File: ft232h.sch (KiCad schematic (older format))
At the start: 0 parts

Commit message: Add schematic of FT232H. Not placed yet.
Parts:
- added C101, C107, C109: 4.7u, Capacitors_SMD:C_0603, symbol C
- added C102, C103, C104, C106, C108, C36, C38, C53, C84: 100n, Capacitors_SMD:C_0603, symbol C
- added C105: 10n, Capacitors_SMD:C_0603, symbol C
- added C110, C111: 20p, Capacitors_SMD:C_0603, symbol C
- added J3: USB_OTG, Connectors:USB_Mini-B, symbol USB_OTG
- added L13, L14: BLM18KG601SN1D, Inductors_SMD:L_0805, symbol Ferrite_Bead
- added R30, R31, R32, R37: 10k, Resistors_SMD:R_0603, symbol R
- added R35: 2k, Resistors_SMD:R_0603, symbol R
- added R36: 12k 1%, Resistors_SMD:R_0603, symbol R
- added U14: FT232HL, Housings_QFP:LQFP-48_7x7mm_Pitch0.5mm, symbol FT232H
- added U15: 93LCxxBT-I/OT, TO_SOT_Packages_SMD:SOT-23-6, symbol 93LCxxBT-I/OT
- added Y3: ABLS2-12.000MHZ-D4Y-T, Crystals:Crystal_HC49-SD_SMD, symbol Crystal
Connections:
- new net: C110.1, U14.1 (XCSI), Y3.1
- new net: C111.1, U14.2 (XCSO), Y3.2
- new net: C53.1, U14.37 (VCCA)
- new net: C38.1, U14.38 (VCCCORE)
- new net: C106.1, C107.1, L13.1, U14.40 (VREGIN)
- new net: R35.1, U14.43 (EEDATA), U15.3 (DI)
- new net: R36.2, U14.5 (REF)
- new net: R32.2, R35.2, U15.1 (DO)
- new net: J3.1 (VBUS), L13.2
- new net 3V3_PLL: C108.1, C109.1, L14.1, U14.3 (VPHY), U14.8 (VPLL)
- new net CS: R31.2, U14.45 (EECS), U15.5 (CS)
- new net DM: J3.2 (D-), U14.6 (DM)
- new net DP: J3.3 (D+), U14.7 (DP)
- new net FT232_3V3: C101.1, C102.1, C103.1, C104.1, C36.1, C84.1, L14.2, R30.1, R31.1, R32.1, R37.1, U14.12 (VCCIO), U14.24 (VCCIO), U14.39 (VCCD), U14.46 (VCCIO), U15.6 (VCC)
- new net GNDD: C101.2, C102.2, C103.2, C104.2, C105.2, C106.2, C107.2, C108.2, C109.2, C110.2, C111.2, C36.2, C38.2, C53.2, C84.2, J3.5 (GND), J3.6 (Shield), R36.1, U14.10 (DGND), U14.11 (DGND), U14.22 (DGND), U14.23 (DGND), U14.35 (DGND), U14.36 (DGND), U14.4 (DGND), U14.41 (DGND), U14.42 (TEST), U14.47 (DGND), U14.48 (DGND), U14.9 (DGND), U15.2 (GND)
- new net SCLK: R30.2, U14.44 (EECLK), U15.4 (SCLK)
- new net ~RST: C105.1, R37.2, U14.34 (~RESET)

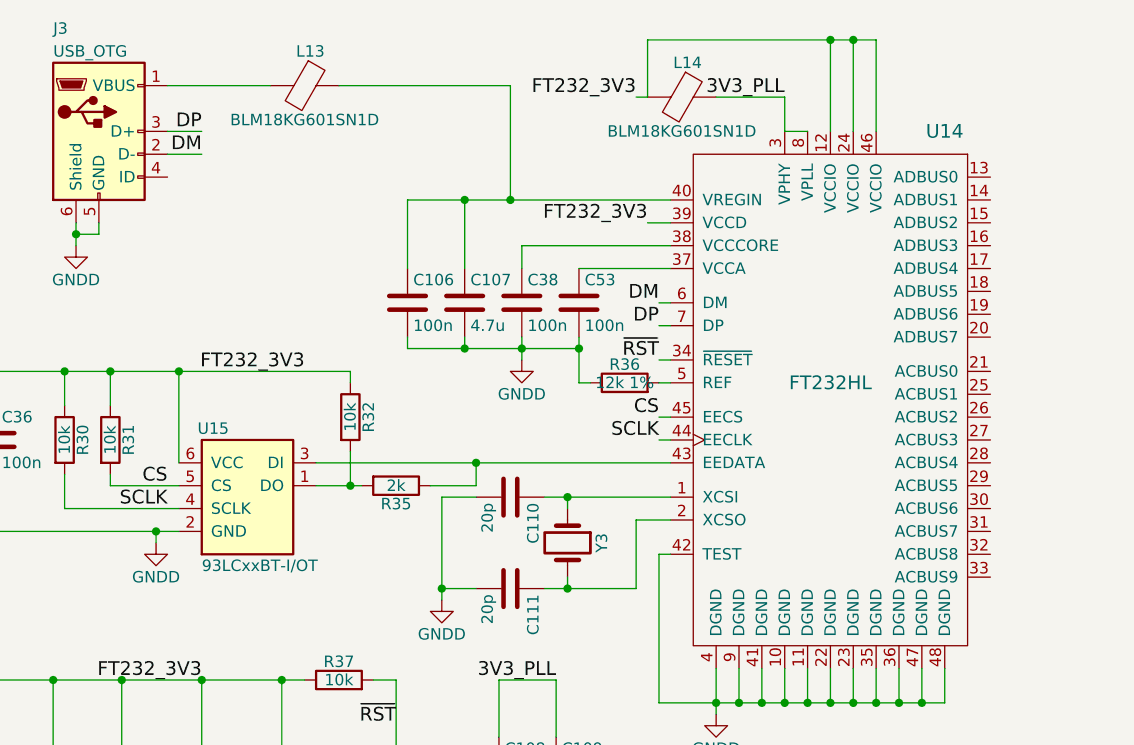
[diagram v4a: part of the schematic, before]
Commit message: FT232H has been finished Not finished: - PROGRAMN button - silkscreen preparation - RF
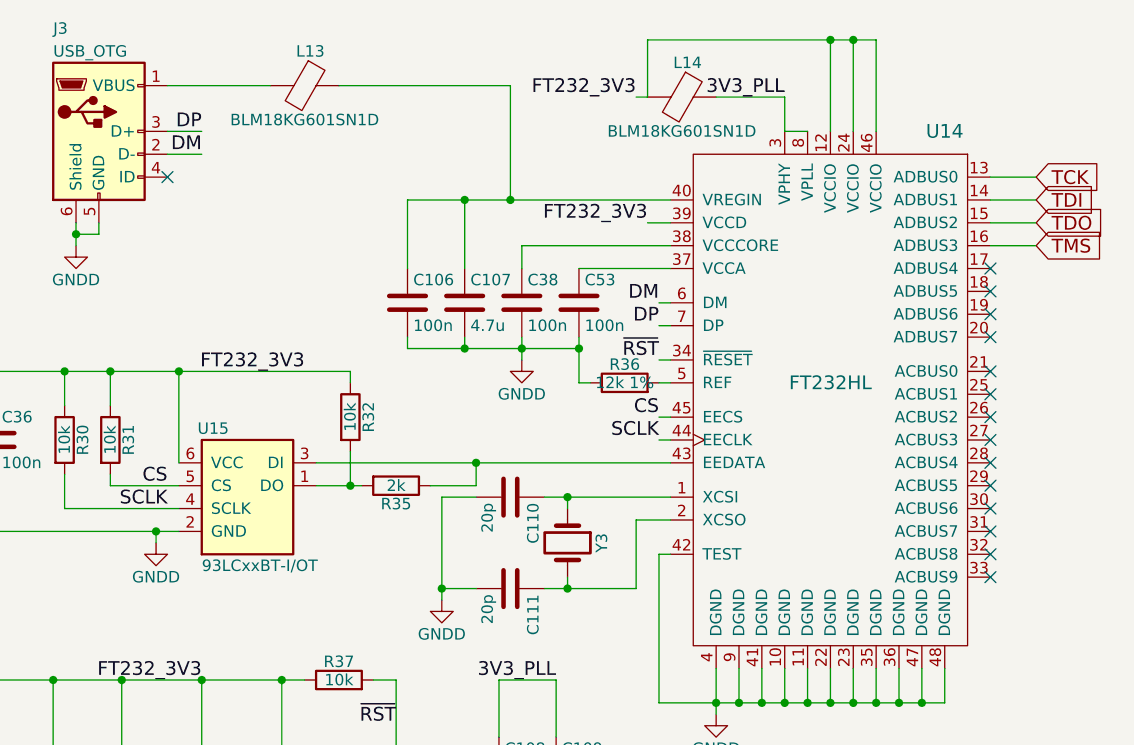
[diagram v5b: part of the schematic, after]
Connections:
- net TCK: now reaches U14.13 (ADBUS0)
- net TDI: now reaches U14.14 (ADBUS1)
- net TDO: now reaches U14.15 (ADBUS2)
- net TMS: now reaches U14.16 (ADBUS3)
- no-connect marks 0 -> 15
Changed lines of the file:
@@
 	3550 3850 3700 3850
 Connection ~ 3250 4150
+Text GLabel 5300 2650 2    60   Input ~ 0
+TMS
+Text GLabel 5300 2450 2    60   Input ~ 0
+TDI
+Text GLabel 5300 2350 2    60   Input ~ 0
+TCK
+Text GLabel 5300 2550 2    60   Input ~ 0
+TDO
+Wire Wire Line
+	5300 2350 5100 2350
+Wire Wire Line
+	5300 2450 5100 2450
+Wire Wire Line
+	5300 2550 5100 2550
+Wire Wire Line
+	5300 2650 5100 2650
+NoConn ~ 5100 2750
+NoConn ~ 5100 2850
+NoConn ~ 5100 2950
+NoConn ~ 5100 3050
+NoConn ~ 5100 3200
+NoConn ~ 5100 3300
+NoConn ~ 5100 3400
+NoConn ~ 5100 3500
+NoConn ~ 5100 3600
+NoConn ~ 5100 3700
+NoConn ~ 5100 3800
+NoConn ~ 5100 3900
+NoConn ~ 5100 4000
+NoConn ~ 5100 4100
+NoConn ~ 1500 2350
 $EndSCHEMATC

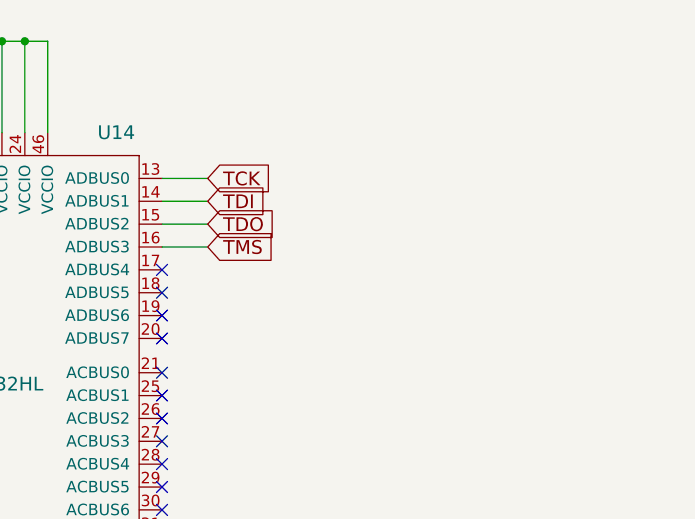
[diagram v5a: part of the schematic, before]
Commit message: Changed JTAG, added 0 Ohm resistors
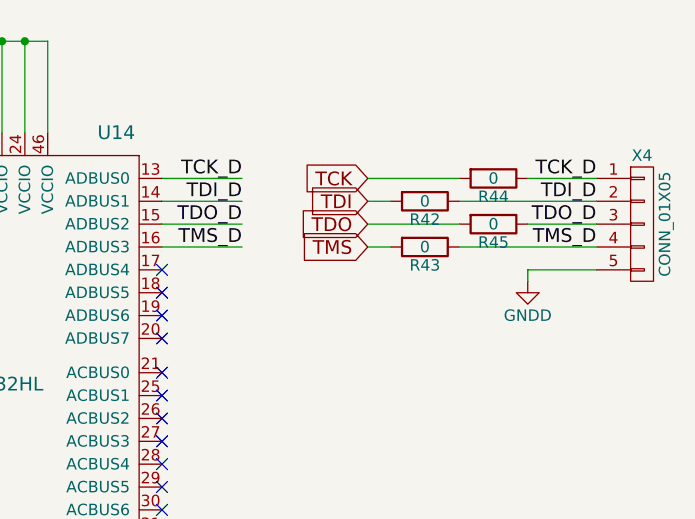
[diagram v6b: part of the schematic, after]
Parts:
- added R42, R43, R44, R45: 0, Resistors_SMD:R_0603, symbol R
- added X4: CONN_01X05, Pin_Headers:Pin_Header_Straight_1x05_Pitch2.00mm, symbol CONN_01X05
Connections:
- net GNDD: now also X4.5 (P5)
- net TCK: now also R44.2; no longer U14.13 (ADBUS0)
- net TDI: now also R42.2; no longer U14.14 (ADBUS1)
- net TDO: now also R45.2; no longer U14.15 (ADBUS2)
- net TMS: now also R43.2; no longer U14.16 (ADBUS3)
- new net TCK_D: R44.1, U14.13 (ADBUS0), X4.1 (P1)
- new net TDI_D: R42.1, U14.14 (ADBUS1), X4.2 (P2)
- new net TDO_D: R45.1, U14.15 (ADBUS2), X4.3 (P3)
- new net TMS_D: R43.1, U14.16 (ADBUS3), X4.4 (P4)
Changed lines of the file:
@@
 	3550 3850 3700 3850
 Connection ~ 3250 4150
-Text GLabel 5300 2650 2    60   Input ~ 0
-TMS
-Text GLabel 5300 2450 2    60   Input ~ 0
-TDI
-Text GLabel 5300 2350 2    60   Input ~ 0
-TCK
-Text GLabel 5300 2550 2    60   Input ~ 0
-TDO
 Wire Wire Line
-	5300 2350 5100 2350
+	5450 2350 5100 2350
 Wire Wire Line
-	5300 2450 5100 2450
+	5450 2450 5100 2450
 Wire Wire Line
-	5300 2550 5100 2550
+	5450 2550 5100 2550
 Wire Wire Line
-	5300 2650 5100 2650
+	5450 2650 5100 2650
 NoConn ~ 5100 2750
 NoConn ~ 5100 2850
@@
 NoConn ~ 5100 4100
 NoConn ~ 1500 2350
+$Comp
+L CONN_01X05 X4
+U 1 1 593E4F67
+P 7200 2550
+F 0 "X4" H 7200 2850 50  0000 C CNN
+F 1 "CONN_01X05" V 7300 2550 50  0000 C CNN
+F 2 "Pin_Headers:Pin_Header_Straight_1x05_Pitch2.00mm" H 7200 2550 50  0001 C CNN
+F 3 "" H 7200 2550 50  0001 C CNN
+	1    7200 2550
+	1    0    0    -1
+$EndComp
+Text GLabel 6000 2650 0    60   Input ~ 0
+TMS
+Text GLabel 6000 2450 0    60   Input ~ 0
+TDI
+Text GLabel 6000 2350 0    60   Input ~ 0
+TCK
+Text GLabel 6000 2550 0    60   Input ~ 0
+TDO
+Wire Wire Line
+	6700 2350 7000 2350
+Wire Wire Line
+	6400 2450 7000 2450
+Wire Wire Line
+	6700 2550 7000 2550
+Wire Wire Line
+	6400 2650 7000 2650
+$Comp
+L GNDD #PWR0104
+U 1 1 593E55E3
+P 6700 2800
+F 0 "#PWR0104" H 6700 2550 50  0001 C CNN
+F 1 "GNDD" H 6700 2650 50  0000 C CNN
+F 2 "" H 6700 2800 50  0001 C CNN
+F 3 "" H 6700 2800 50  0001 C CNN
+	1    6700 2800
+	1    0    0    -1
+$EndComp
+Wire Wire Line
+	6700 2800 6700 2750
+Wire Wire Line
+	6700 2750 7000 2750
+$Comp
+L R R44
+U 1 1 593EA9DA
+P 6550 2350
+F 0 "R44" V 6630 2350 50  0000 C CNN
+F 1 "0" V 6550 2350 50  0000 C CNN
+F 2 "Resistors_SMD:R_0603" V 6480 2350 50  0001 C CNN
+F 3 "" H 6550 2350 50  0001 C CNN
+	1    6550 2350
+	0    1    1    0
+$EndComp
+$Comp
+L R R43
+U 1 1 593EAB87
+P 6250 2650
+F 0 "R43" V 6330 2650 50  0000 C CNN
+F 1 "0" V 6250 2650 50  0000 C CNN
+F 2 "Resistors_SMD:R_0603" V 6180 2650 50  0001 C CNN
+F 3 "" H 6250 2650 50  0001 C CNN
+	1    6250 2650
+	0    1    1    0
+$EndComp
+$Comp
+L R R42
+U 1 1 593EAC51
+P 6250 2450
+F 0 "R42" V 6330 2450 50  0000 C CNN
+F 1 "0" V 6250 2450 50  0000 C CNN
+F 2 "Resistors_SMD:R_0603" V 6180 2450 50  0001 C CNN
+F 3 "" H 6250 2450 50  0001 C CNN
+	1    6250 2450
+	0    1    1    0
+$EndComp
+$Comp
+L R R45
+U 1 1 593EACDA
+P 6550 2550
+F 0 "R45" V 6630 2550 50  0000 C CNN
+F 1 "0" V 6550 2550 50  0000 C CNN
+F 2 "Resistors_SMD:R_0603" V 6480 2550 50  0001 C CNN
+F 3 "" H 6550 2550 50  0001 C CNN
+	1    6550 2550
+	0    1    1    0
+$EndComp
+Wire Wire Line
+	6400 2350 6000 2350
+Wire Wire Line
+	6000 2450 6100 2450
+Wire Wire Line
+	6000 2550 6400 2550
+Wire Wire Line
+	6100 2650 6000 2650
+Text Label 5450 2350 2    60   ~ 0
+TCK_D
+Text Label 5450 2450 2    60   ~ 0
+TDI_D
+Text Label 5450 2550 2    60   ~ 0
+TDO_D
+Text Label 5450 2650 2    60   ~ 0
+TMS_D
+Text Label 7000 2350 2    60   ~ 0
+TCK_D
+Text Label 7000 2450 2    60   ~ 0
+TDI_D
+Text Label 7000 2550 2    60   ~ 0
+TDO_D
+Text Label 7000 2650 2    60   ~ 0
+TMS_D
 $EndSCHEMATC

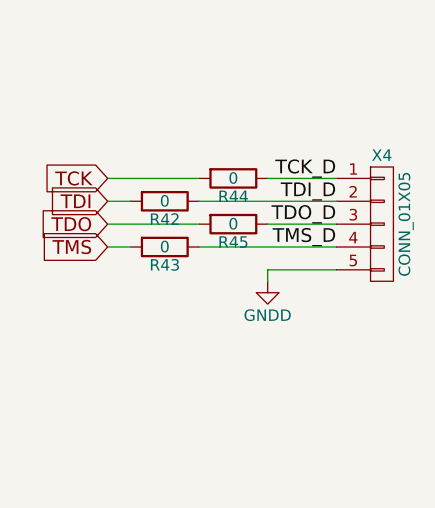
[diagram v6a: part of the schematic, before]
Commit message: Finish silkscreen layer.
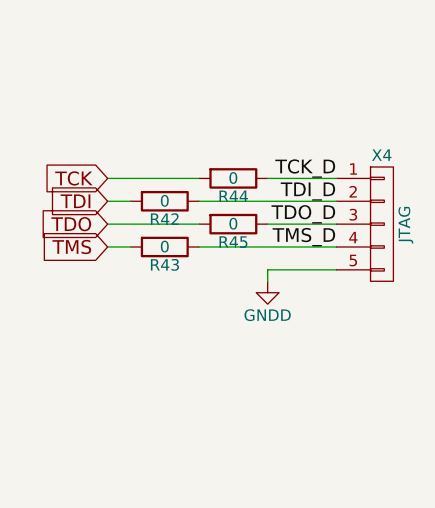
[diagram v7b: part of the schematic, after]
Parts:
- X4: value CONN_01X05 -> JTAG
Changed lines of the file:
@@
 P 7200 2550
 F 0 "X4" H 7200 2850 50  0000 C CNN
-F 1 "CONN_01X05" V 7300 2550 50  0000 C CNN
+F 1 "JTAG" V 7300 2550 50  0000 C CNN
 F 2 "Pin_Headers:Pin_Header_Straight_1x05_Pitch2.00mm" H 7200 2550 50  0001 C CNN
 F 3 "" H 7200 2550 50  0001 C CNN

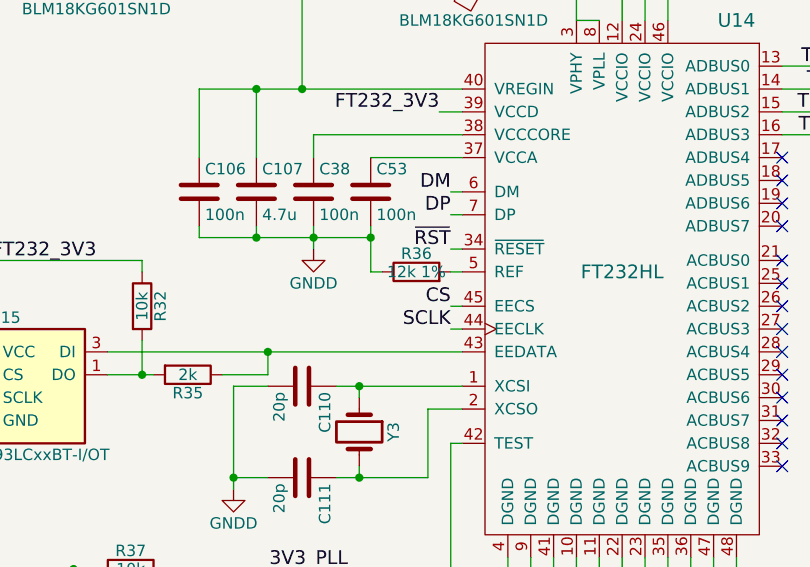
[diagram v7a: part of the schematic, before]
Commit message: Prepared BOM and changed some part numbers for unpopular ones. Added manufacture PN for each part.
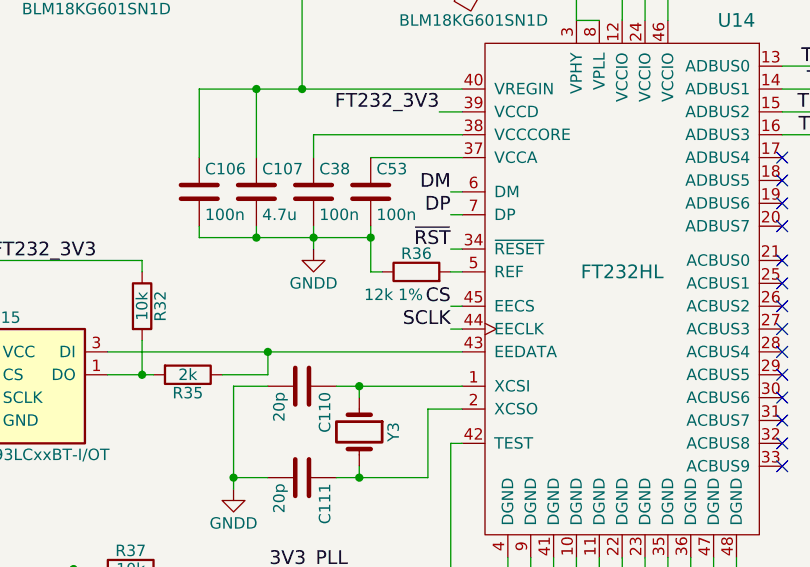
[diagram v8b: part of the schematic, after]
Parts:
- J3: manf# (none) -> UX60-MB-5ST
- L14: manf# (none) -> BLM18KG601SN1D
- R35: manf# (none) -> RC0603JR-072KL
- R36: manf# (none) -> RC0603FR-0712RL
- R44: manf# (none) -> RC0603JR-070RL
- U14: manf# (none) -> FT232HL
- U15: manf# (none) -> 93LC56BT-I/OT
- X4: manf# (none) -> NRPN201PAEN-RC
- Y3: manf# (none) -> ABLS2-12.000MHZ-D4Y-T
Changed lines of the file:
@@
 LIBS:valves
 LIBS:sdr
-LIBS:usb-type-c
 LIBS:sdr-cache
 EELAYER 25 0
@@
 F 2 "Housings_QFP:LQFP-48_7x7mm_Pitch0.5mm" H 5750 4850 60  0001 C CNN
 F 3 "" H 5750 4850 60  0001 C CNN
+F 4 "FT232HL" H 4350 4400 60  0001 C CNN "manf#"
 	1    4350 4400
 	1    0    0    -1
@@
 F 2 "Resistors_SMD:R_0603" V 2430 3700 50  0001 C CNN
 F 3 "" H 2500 3700 50  0001 C CNN
+F 4 "RC0603JR-072KL" H 2500 3700 60  0001 C CNN "manf#"
 	1    2500 3700
 	0    1    1    0
@@
 F 2 "Connectors:USB_Mini-B" H 1350 2100 50  0001 C CNN
 F 3 "" H 1350 2100 50  0001 C CNN
+F 4 "UX60-MB-5ST" H 1200 2150 60  0001 C CNN "manf#"
 	1    1200 2150
 	1    0    0    -1
@@
 F 2 "Inductors_SMD:L_0805" V 3680 2000 50  0001 C CNN
 F 3 "" H 3750 2000 50  0001 C CNN
+F 4 "BLM18KG601SN1D" H 3750 2000 60  0001 C CNN "manf#"
 	1    3750 2000
 	0    1    1    0
@@
 F 2 "TO_SOT_Packages_SMD:SOT-23-6" H 1850 3400 50  0001 C CNN
 F 3 "" H 1850 3900 50  0001 C CNN
+F 4 "93LC56BT-I/OT" H 1850 3800 60  0001 C CNN "manf#"
 	1    1850 3800
 	1    0    0    -1
@@
 P 3500 3250
 F 0 "R36" V 3580 3250 50  0000 C CNN
-F 1 "12k 1%" V 3500 3250 50  0000 C CNN
+F 1 "12k 1%" V 3400 3350 50  0000 C CNN
 F 2 "Resistors_SMD:R_0603" V 3430 3250 50  0001 C CNN
 F 3 "" H 3500 3250 50  0001 C CNN
+F 4 "RC0603FR-0712RL" H 3500 3250 60  0001 C CNN "manf#"
 	1    3500 3250
 	0    -1   -1   0
@@
 F 2 "Crystals:Crystal_HC49-SD_SMD" H 3250 3950 50  0001 C CNN
 F 3 "" H 3250 3950 50  0001 C CNN
+F 4 "ABLS2-12.000MHZ-D4Y-T" H 3250 3950 60  0001 C CNN "manf#"
 	1    3250 3950
 	0    1    1    0
@@
 F 2 "Pin_Headers:Pin_Header_Straight_1x05_Pitch2.00mm" H 7200 2550 50  0001 C CNN
 F 3 "" H 7200 2550 50  0001 C CNN
+F 4 "NRPN201PAEN-RC" H 7200 2550 60  0001 C CNN "manf#"
 	1    7200 2550
 	1    0    0    -1
@@
 F 2 "Resistors_SMD:R_0603" V 6480 2350 50  0001 C CNN
 F 3 "" H 6550 2350 50  0001 C CNN
+F 4 "RC0603JR-070RL" H 6550 2350 60  0001 C CNN "manf#"
 	1    6550 2350
 	0    1    1    0
